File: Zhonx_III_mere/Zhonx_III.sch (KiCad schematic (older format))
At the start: 133 parts, among them K1 L_Motor, K2 R_Motor, K3 USART, P1 JTAG, Q1 FDV301N, Q2 FDV301N, U1 MCP73213, U10 BSL214N, U11 BSL214N, U12 24LC64T, U14 STM32F405RGT6, U16 Line_1, U17 Line_2, U18 Line_3, U19 Line_4, U2 A3918_L, U20 Line_5, U3 A3918_R, U4 LTC2955CTS8-2, U5 SIB911DK, U6 SI1551DL, U7 LM2940, U8 MCP1700, U9 MCP1700, X1 QUARTZ_8Z

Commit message: Update schematic libs
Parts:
- C1, C10, C11, C12, C13, C14, C15, C16, C17, C18, C19, C2, C20, C21, C22, C23, C24, C25, C26, C27, C28, C29, C3, C30, C31, C32, C33, C34, C35, C36, C37, C38, C39, C4, C40, C41, C43, C44, C45, C5, C6, C7, C8, C9: symbol C -> C-RESCUE-Zhonx_III
- C100, C101, C103, C104, C42: symbol CP1 -> CP1-RESCUE-Zhonx_III
- D11, D12: symbol LED -> LED-RESCUE-Zhonx_III
- L2: footprint ~ -> SM0603
- R1, R10, R11, R12, R13, R14, R15, R16, R17, R18, R19, R2, R20, R21, R22, R23, R24, R25, R26, R27, R28, R29, R3, R30, R31, R32, R33, R34, R35, R38, R39, R4, R44, R45, R48, R49, R5, R50, R51, R52, R58, R6, R64, R67, R7, R8, R9: symbol R -> R-RESCUE-Zhonx_III

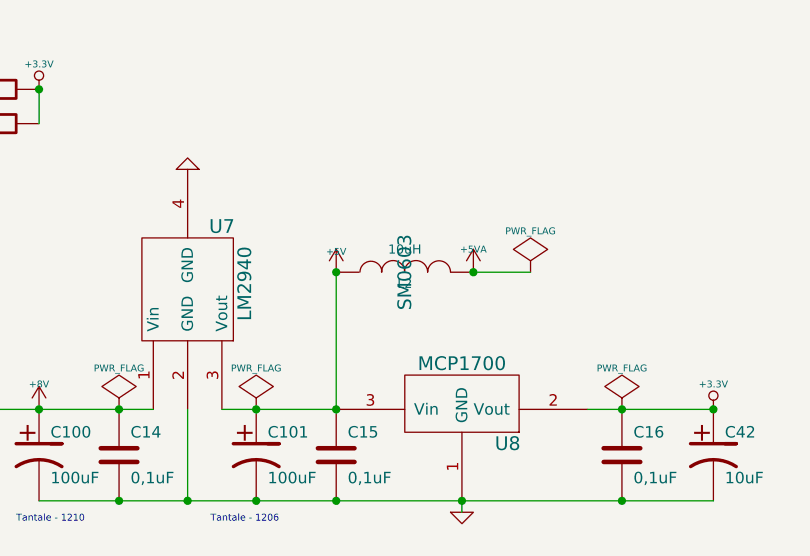
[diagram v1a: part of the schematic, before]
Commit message: repair mod librairies
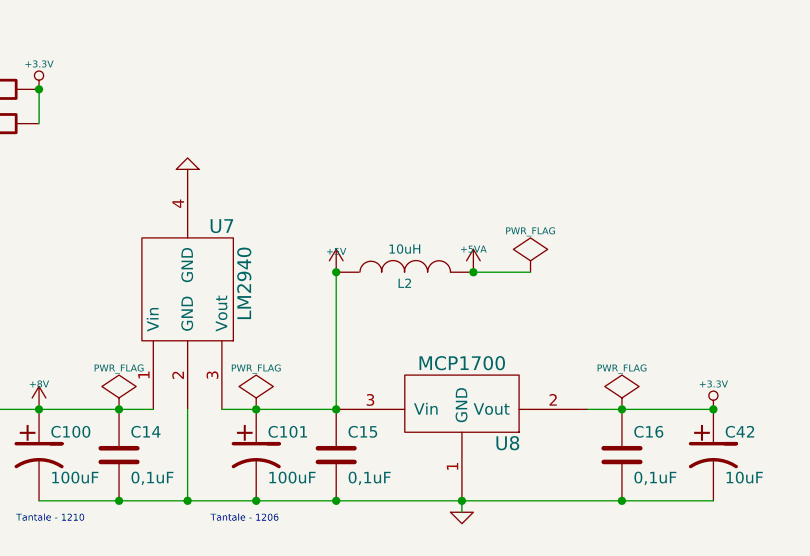
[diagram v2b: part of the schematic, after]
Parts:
- ADXR1: footprint ~ -> kicad_lib:ADXRS620
- C1, C10, C11, C12, C13, C14, C15, C16, C20, C21, C23, C24, C25, C26, C27, C28, C29, C3, C34, C35, C36, C37, C38, C39, C4, C40, C41, C43, C45, C5, C6, C7, C8, C9, R1, R11, R12, R13, R14, R15, R16, R17, R18, R19, R2, R22, R23, R29, R38, R44, R45, R48, R49, R50, R51, R52, R58, R6, R64, R67, R7, R9: footprint (none) -> kicad_lib:SM0402_ZHONX
- C100: footprint (none) -> kicad_lib:SM1210_Capa
- C101, C103, C104: footprint (none) -> kicad_lib:SM1206_Capa
- C17, C18, C19, C2, C22, C30, C31, C32, C33, C44, R10, R20, R21, R24, R25, R26, R3, R30, R31, R32, R33, R4, R5, R8: footprint ~ -> kicad_lib:SM0402_ZHONX
- C42: footprint (none) -> kicad_lib:SM0603_Capa
- D1: footprint ~ -> kicad_lib:SM0603
- D11, D12: footprint (none) -> kicad_lib:LED-0603
- IR1: footprint (none) -> kicad_lib:IR_LF
- IR2: footprint (none) -> kicad_lib:IR_LD
- IR3: footprint (none) -> kicad_lib:IR_RD
- IR4: footprint (none) -> kicad_lib:IR_RF
- K1, K2: footprint (none) -> kicad_lib:Connecteur_Moteur_Zhonx
- K3: footprint (none) -> kicad_lib:Conn_Serial_Zhonx
- L2: footprint SM0603 -> kicad_lib:SM0603
- P1: footprint (none) -> kicad_lib:Zhonx_III_JTAG
- PL1: footprint ~ -> kicad_lib:Platine_Zhonx_III
- Q1, Q2: footprint ~ -> kicad_lib:SOT23GDS
- R27, R28: footprint ~ -> kicad_lib:SM0603_ZHONX
- R34, R35, R39: footprint (none) -> kicad_lib:SM0603_ZHONX
- SCH1: footprint (none) -> kicad_lib:SOD323
- SP1: footprint ~ -> kicad_lib:Buzzer_KSSG13J12
- U1: footprint (none) -> kicad_lib:MCP73213
- U10, U11: footprint (none) -> kicad_lib:SOT23_6
- U12: footprint (none) -> kicad_lib:SOT23-5
- U14: footprint (none) -> kicad_lib:TQFP_64
- U16, U17, U18, U19, U20: footprint (none) -> kicad_lib:QRE1113GR
- U2, U3: footprint ~ -> kicad_lib:QFN16_Termal_Pad
- U4: footprint (none) -> kicad_lib:LTC2955
- U5: footprint ~ -> kicad_lib:SC75-6L
- U6: footprint ~ -> kicad_lib:SC70
- U7: footprint (none) -> kicad_lib:SOT223
- U8, U9: footprint (none) -> kicad_lib:SOT23
- X1: footprint (none) -> kicad_lib:Quartz_8Z-16MHz

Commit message: rename libs
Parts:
- ADXR1: footprint kicad_lib:ADXRS620 -> zhonx_lib:ADXRS620
- C1, C10, C11, C12, C13, C14, C15, C16, C17, C18, C19, C2, C20, C21, C22, C23, C24, C25, C26, C27, C28, C29, C3, C30, C31, C32, C33, C34, C35, C36, C37, C38, C39, C4, C40, C41, C43, C44, C45, C5, C6, C7, C8, C9, R1, R10, R11, R12, R13, R14, R15, R16, R17, R18, R19, R2, R20, R21, R22, R23, R24, R25, R26, R29, R3, R30, R31, R32, R33, R38, R4, R44, R45, R48, R49, R5, R50, R51, R52, R58, R6, R64, R67, R7, R8, R9: footprint kicad_lib:SM0402_ZHONX -> zhonx_lib:SM0402_ZHONX
- C100: footprint kicad_lib:SM1210_Capa -> zhonx_lib:SM1210_Capa
- C101, C103, C104: footprint kicad_lib:SM1206_Capa -> zhonx_lib:SM1206_Capa
- C42: footprint kicad_lib:SM0603_Capa -> zhonx_lib:SM0603_Capa
- D1, L2: footprint kicad_lib:SM0603 -> zhonx_lib:SM0603
- D11, D12: footprint kicad_lib:LED-0603 -> zhonx_lib:LED-0603
- IR1: footprint kicad_lib:IR_LF -> zhonx_lib:IR_LF
- IR2: footprint kicad_lib:IR_LD -> zhonx_lib:IR_LD
- IR3: footprint kicad_lib:IR_RD -> zhonx_lib:IR_RD
- IR4: footprint kicad_lib:IR_RF -> zhonx_lib:IR_RF
- K1, K2: footprint kicad_lib:Connecteur_Moteur_Zhonx -> zhonx_lib:Connecteur_Moteur_Zhonx
- K3: footprint kicad_lib:Conn_Serial_Zhonx -> zhonx_lib:Conn_Serial_Zhonx
- P1: footprint kicad_lib:Zhonx_III_JTAG -> zhonx_lib:Zhonx_III_JTAG
- PL1: footprint kicad_lib:Platine_Zhonx_III -> zhonx_lib:Platine_Zhonx_III
- Q1, Q2: footprint kicad_lib:SOT23GDS -> zhonx_lib:SOT23GDS
- R27, R28, R34, R35, R39: footprint kicad_lib:SM0603_ZHONX -> zhonx_lib:SM0603_ZHONX
- SCH1: footprint kicad_lib:SOD323 -> zhonx_lib:SOD323
- SP1: footprint kicad_lib:Buzzer_KSSG13J12 -> zhonx_lib:Buzzer_KSSG13J12
- U1: footprint kicad_lib:MCP73213 -> zhonx_lib:MCP73213
- U10, U11: footprint kicad_lib:SOT23_6 -> zhonx_lib:SOT23_6
- U12: footprint kicad_lib:SOT23-5 -> zhonx_lib:SOT23-5
- U14: footprint kicad_lib:TQFP_64 -> zhonx_lib:TQFP_64
- U16, U17, U18, U19, U20: footprint kicad_lib:QRE1113GR -> zhonx_lib:QRE1113GR
- U2, U3: footprint kicad_lib:QFN16_Termal_Pad -> zhonx_lib:QFN16_Termal_Pad
- U4: footprint kicad_lib:LTC2955 -> zhonx_lib:LTC2955
- U5: footprint kicad_lib:SC75-6L -> zhonx_lib:SC75-6L
- U6: footprint kicad_lib:SC70 -> zhonx_lib:SC70
- U7: footprint kicad_lib:SOT223 -> zhonx_lib:SOT223
- U8, U9: footprint kicad_lib:SOT23 -> zhonx_lib:SOT23
- X1: footprint kicad_lib:Quartz_8Z-16MHz -> zhonx_lib:Quartz_8Z-16MHz

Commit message: update lib settigns
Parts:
- PL1: symbol PLATINE_ZHONX_III -> PLATINE_ZHONX_III-RESCUE-Zhonx_III
- U1: symbol MCP73213 -> MCP73213-RESCUE-Zhonx_III
- U4: symbol LTC2955TS8-2 -> LTC2955TS8-2-RESCUE-Zhonx_III
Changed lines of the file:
@@
 EESchema Schematic File Version 2
+LIBS:Zhonx_III-rescue
+LIBS:Librairies_STM32
+LIBS:Librairies_Zhonx
 LIBS:Zhonx_III-cache
 EELAYER 25 0
@@
 $EndComp
 $Comp
-L LTC2955TS8-2 U4
+L LTC2955TS8-2-RESCUE-Zhonx_III U4
 U 1 1 518528A3
 P 2850 1000
@@
 $EndComp
 $Comp
-L MCP73213 U1
+L MCP73213-RESCUE-Zhonx_III U1
 U 1 1 518528E4
 P 1900 3300
@@
 $EndComp
 $Comp
-L PLATINE_ZHONX_III PL1
+L PLATINE_ZHONX_III-RESCUE-Zhonx_III PL1
 U 1 1 51891F86
 P 7250 7800
